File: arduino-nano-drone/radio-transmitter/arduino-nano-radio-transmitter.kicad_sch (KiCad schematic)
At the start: 8 parts, among them J1 Conn_01x04_Pin, J2 Conn_01x04_Pin, J3 Conn_01x04_Pin, U2 AMS1117-3.3, U3 NRF24L01_Breakout

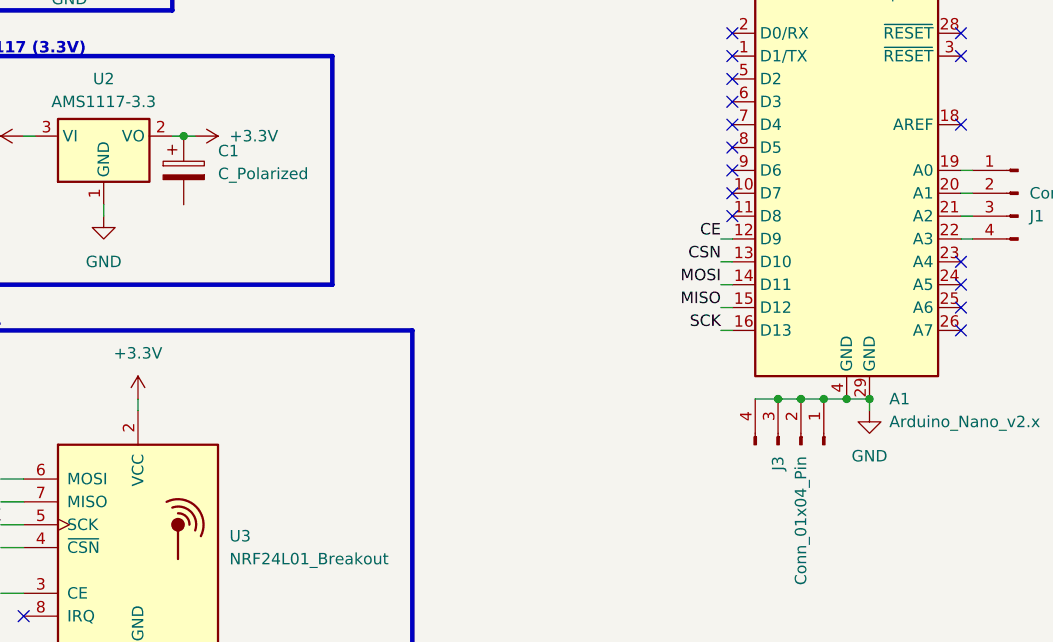
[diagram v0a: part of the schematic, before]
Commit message: project 8 / arduino nano drone / added rt, rr, fl pcb, improved layout
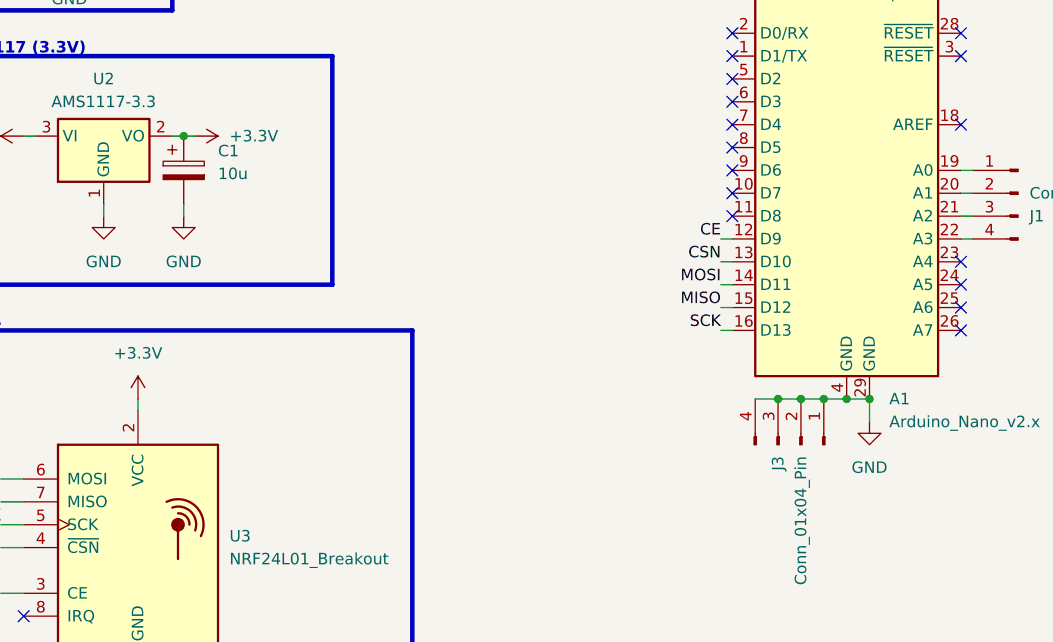
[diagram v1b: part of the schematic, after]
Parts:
- BT1: footprint (none) -> Connector_PinHeader_2.54mm:PinHeader_1x02_P2.54mm_Vertical
- C1: value C_Polarized -> 10u; footprint (none) -> Capacitor_THT:CP_Radial_D4.0mm_P1.50mm
- J1, J2, J3: footprint (none) -> Connector_PinHeader_2.54mm:PinHeader_1x04_P2.54mm_Vertical
- U2: footprint Package_TO_SOT_SMD:SOT-223-3_TabPin2 -> Connector_PinSocket_2.54mm:PinSocket_1x03_P2.54mm_Vertical
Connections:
- net GND: now also C1.2
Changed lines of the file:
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@@
     (stroke (width 0) (type default))
   )
-  (wire (pts (xy 116.84 88.9) (xy 116.84 90.17))
+  (wire (pts (xy 116.84 88.9) (xy 116.84 91.44))
     (stroke (width 0) (type default))
   )
@@
   )
   (wire (pts (xy 106.68 88.9) (xy 104.14 88.9))
+    (stroke (width 0) (type default))
+  )
+  (wire (pts (xy 40.64 68.58) (xy 40.64 67.31))
     (stroke (width 0) (type default))
   )
@@
       (effects (font (size 1.27 1.27)))
     )
-    (property "Footprint" "Package_TO_SOT_SMD:SOT-223-3_TabPin2" (at 31.75 54.61 0)
+    (property "Footprint" "Connector_PinSocket_2.54mm:PinSocket_1x03_P2.54mm_Vertical" (at 31.75 54.61 0)
       (effects (font (size 1.27 1.27)) hide)
     )
@@
       (effects (font (size 1.27 1.27)) (justify left))
     )
-    (property "Footprint" "" (at 27.94 30.226 90)
+    (property "Footprint" "Connector_PinHeader_2.54mm:PinHeader_1x02_P2.54mm_Vertical" (at 27.94 30.226 90)
       (effects (font (size 1.27 1.27)) hide)
     )
@@
     )
   )
-  (symbol (lib_id "power:GND") (at 116.84 90.17 0) (unit 1)
-    (in_bom yes) (on_board yes) (dnp no) (fields_autoplaced)
-    (property "Reference" "#PWR07" (at 116.84 96.52 0)
-      (effects (font (size 1.27 1.27)) hide)
-    )
-    (property "Value" "GND" (at 116.84 95.25 0)
-      (effects (font (size 1.27 1.27)))
-    )
-    (property "Footprint" "" (at 116.84 90.17 0)
-      (effects (font (size 1.27 1.27)) hide)
-    )
-    (property "Datasheet" "" (at 116.84 90.17 0)
+  (symbol (lib_id "power:GND") (at 116.84 91.44 0) (unit 1)
+    (in_bom yes) (on_board yes) (dnp no) (fields_autoplaced)
+    (property "Reference" "#PWR07" (at 116.84 97.79 0)
+      (effects (font (size 1.27 1.27)) hide)
+    )
+    (property "Value" "GND" (at 116.84 96.52 0)
+      (effects (font (size 1.27 1.27)))
+    )
+    (property "Footprint" "" (at 116.84 91.44 0)
+      (effects (font (size 1.27 1.27)) hide)
+    )
+    (property "Datasheet" "" (at 116.84 91.44 0)
       (effects (font (size 1.27 1.27)) hide)
     )
@@
       (effects (font (size 1.27 1.27)) (justify left))
     )
-    (property "Value" "C_Polarized" (at 44.45 63.881 0)
-      (effects (font (size 1.27 1.27)) (justify left))
-    )
-    (property "Footprint" "" (at 41.6052 67.31 0)
+    (property "Value" "10u" (at 44.45 63.881 0)
+      (effects (font (size 1.27 1.27)) (justify left))
+    )
+    (property "Footprint" "Capacitor_THT:CP_Radial_D4.0mm_P1.50mm" (at 41.6052 67.31 0)
       (effects (font (size 1.27 1.27)) hide)
     )
@@
       (effects (font (size 1.27 1.27)) (justify right))
     )
-    (property "Footprint" "" (at 133.35 66.04 0)
+    (property "Footprint" "Connector_PinHeader_2.54mm:PinHeader_1x04_P2.54mm_Vertical" (at 133.35 66.04 0)
       (effects (font (size 1.27 1.27)) hide)
     )
@@
       (effects (font (size 1.27 1.27)) (justify right))
     )
-    (property "Footprint" "" (at 121.92 30.48 0)
+    (property "Footprint" "Connector_PinHeader_2.54mm:PinHeader_1x04_P2.54mm_Vertical" (at 121.92 30.48 0)
       (effects (font (size 1.27 1.27)) hide)
     )
@@
       (effects (font (size 1.27 1.27)) (justify right))
     )
-    (property "Footprint" "" (at 109.22 93.98 0)
+    (property "Footprint" "Connector_PinHeader_2.54mm:PinHeader_1x04_P2.54mm_Vertical" (at 109.22 93.98 0)
       (effects (font (size 1.27 1.27)) hide)
     )
@@
         )
       )
+    )
+  )
+  (symbol (lib_id "power:GND") (at 40.64 68.58 0) (unit 1)
+    (in_bom yes) (on_board yes) (dnp no) (fields_autoplaced)
+    (property "Reference" "#PWR010" (at 40.64 74.93 0)
+      (effects (font (size 1.27 1.27)) hide)
+    )
+    (property "Value" "GND" (at 40.64 73.66 0)
+      (effects (font (size 1.27 1.27)))
+    )
+    (property "Footprint" "" (at 40.64 68.58 0)
+      (effects (font (size 1.27 1.27)) hide)
+    )
+    (property "Datasheet" "" (at 40.64 68.58 0)
+      (effects (font (size 1.27 1.27)) hide)
+    )
+    (pin "1")
+    (instances
+      (project "arduino-nano-radio-transmitter"
+        (path "/d9490172-cce4-4de5-848d-de895285794a"
+          (reference "#PWR010") (unit 1)
+        )
+      )

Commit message: Reviewed schematics and boards
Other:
- note added: "ALE upewnij się, czy mówię dobrze, bo mogłem pomylić wersje arduino"
- note added: "IMO nierozsądnym jest nieprowadzić pinu IRQ. Możesz go nie użyć w kodzie, ale dobrze zostawić sobie taką możliwość."
- note added: "Jak dobrze kojarzę, to na tych arduino siedzi AMS. Czemu nie zasilać prosto z pinu 3.3V? Nie masz raczej tak dużych prądów"
- note added: "Owszem, według specki powinno przyjąć 12.6V, ale poczytaj fora. Przy 12V te układy lubią padać. Szczególnie jak jest to niestabilne 12V"
- note added: "RF ma to do siebie, że jest bardzo wrażliwe na zasilanie. Dodałbym kondek 1-10uF przy samiutkim złączu radia"
- note added: "Szczególnie, że robienie RF (a tym bardziej drona) bez przerwań, nie wydaje się zbyt mądre :)"
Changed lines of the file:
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@@
     (fill (type none))
+  )
+  (text "RF ma to do siebie, że jest bardzo wrażliwe na zasilanie. Dodałbym kondek 1-10uF przy samiutkim złączu radia"
+    (at 39.37 90.17 0)
+    (effects (font (size 1.27 1.27) (color 255 32 34 1)) (justify left bottom))
+  )
+  (text "ALE upewnij się, czy mówię dobrze, bo mogłem pomylić wersje arduino"
+    (at 48.26 62.23 0)
+    (effects (font (size 1.27 1.27) (color 255 4 0 1)) (justify left bottom))
   )
   (text "BATTERY" (at 13.97 16.51 0)
     (effects (font (size 1.27 1.27) (thickness 0.254) bold (color 0 0 0 1)) (justify left bottom))
   )
+  (text "Szczególnie, że robienie RF (a tym bardziej drona) bez przerwań, nie wydaje się zbyt mądre :)"
+    (at 19.05 118.11 0)
+    (effects (font (size 1.27 1.27) (color 255 0 8 1)) (justify left bottom))
+  )
   (text "NRF24" (at 13.97 81.28 0)
     (effects (font (size 1.27 1.27) (thickness 0.254) bold (color 0 0 0 1)) (justify left bottom))
+  )
+  (text "Owszem, według specki powinno przyjąć 12.6V, ale poczytaj fora. Przy 12V te układy lubią padać. Szczególnie jak jest to niestabilne 12V"
+    (at 88.9 30.48 0)
+    (effects (font (size 1.27 1.27) (color 255 10 19 1)) (justify left bottom))
   )
   (text "AMS1117 (3.3V)" (at 13.97 50.8 0)
     (effects (font (size 1.27 1.27) (thickness 0.254) bold (color 0 0 0 1)) (justify left bottom))
   )
+  (text "Jak dobrze kojarzę, to na tych arduino siedzi AMS. Czemu nie zasilać prosto z pinu 3.3V? Nie masz raczej tak dużych prądów"
+    (at 40.64 58.42 0)
+    (effects (font (size 1.27 1.27) (color 255 0 15 1)) (justify left bottom))
+  )
+  (text "IMO nierozsądnym jest nieprowadzić pinu IRQ. Możesz go nie użyć w kodzie, ale dobrze zostawić sobie taką możliwość. "
+    (at 19.05 115.57 0)
+    (effects (font (size 1.27 1.27) (color 255 32 34 1)) (justify left bottom))
+  )
   (label "MOSI" (at 20.32 97.79 180) (fields_autoplaced)

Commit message: project 8 / arduino nano drone / improved schematics, pcb after review
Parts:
- added C2: 10u, Capacitor_THT:CP_Radial_D4.0mm_P1.50mm, symbol Device:C_Polarized
- added C3: 100n, Capacitor_THT:C_Disc_D3.0mm_W1.6mm_P2.50mm, symbol Device:C
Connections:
- net +12V: now also C3.2
- net +3.3V: now also C2.1
- net GND: now also C2.2, C3.1
- net IRQ: now reaches A1.11 (D8)
- net IRQ: now also U3.8 (IRQ)
- no-connect marks 18 -> 16
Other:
- note removed: "ALE upewnij się, czy mówię dobrze, bo mogłem pomylić wersje arduino"
- note removed: "IMO nierozsądnym jest nieprowadzić pinu IRQ. Możesz go nie użyć w kodzie, ale dobrze zostawić sobie taką możliwość."
- note removed: "Jak dobrze kojarzę, to na tych arduino siedzi AMS. Czemu nie zasilać prosto z pinu 3.3V? Nie masz raczej tak dużych prądów"
- note removed: "Owszem, według specki powinno przyjąć 12.6V, ale poczytaj fora. Przy 12V te układy lubią padać. Szczególnie jak jest to niestabilne 12V"
- note removed: "RF ma to do siebie, że jest bardzo wrażliwe na zasilanie. Dodałbym kondek 1-10uF przy samiutkim złączu radia"
- note removed: "Szczególnie, że robienie RF (a tym bardziej drona) bez przerwań, nie wydaje się zbyt mądre :)"
